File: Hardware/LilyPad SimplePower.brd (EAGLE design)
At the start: 28.4 x 28.4 mm, 20 parts, among them U1 MCP73831

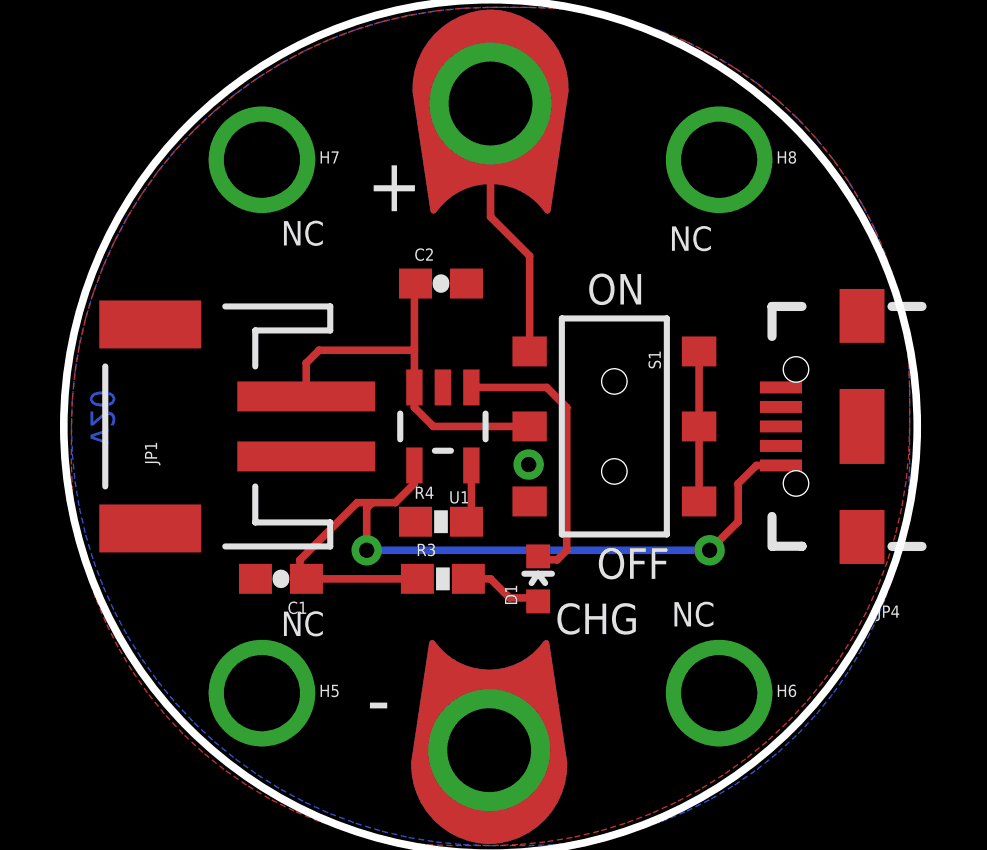
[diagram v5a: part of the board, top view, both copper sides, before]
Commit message: Updating bRestrict to give Lilypad petal pattern
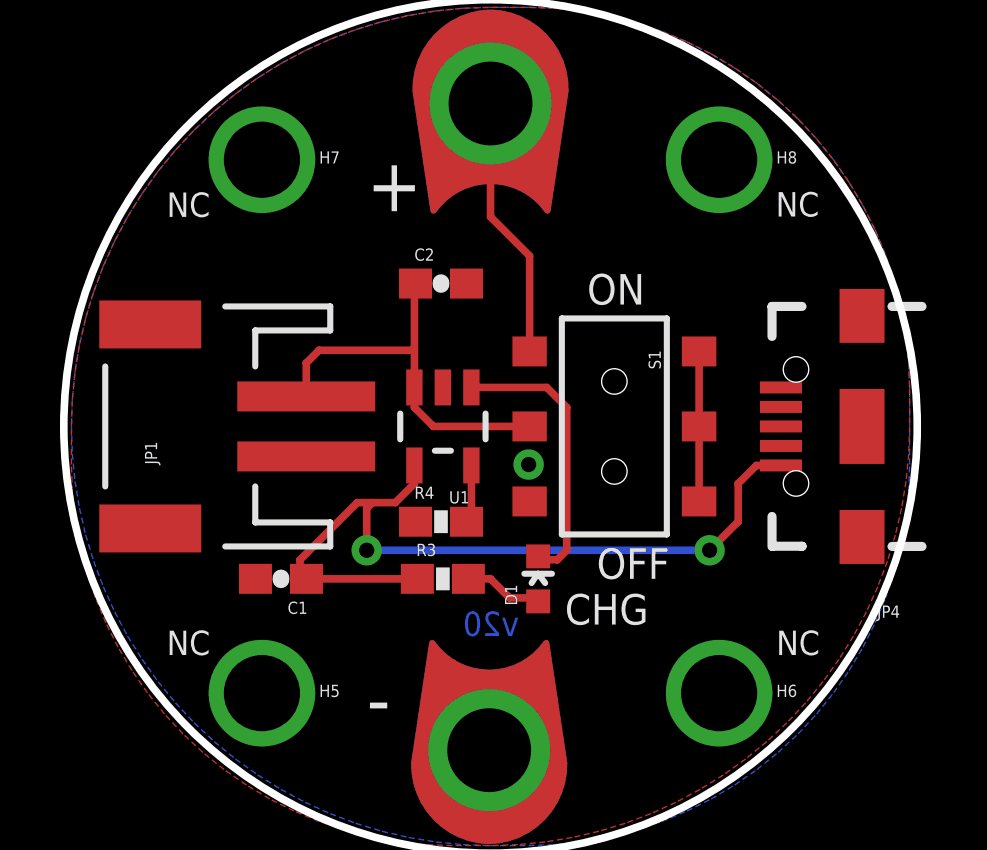
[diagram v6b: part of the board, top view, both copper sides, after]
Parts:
- moved JP3 0.81 mm to (6.51, -4.29)
- moved U$5 0.79 mm to (-5.24, -2.54)
- moved U$1 0.35 mm to (0.16, 1.91)
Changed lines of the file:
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@@
 <layer number="47" name="Measures" color="7" fill="1" visible="no" active="yes"/>
 <layer number="48" name="Document" color="7" fill="1" visible="no" active="yes"/>
-<layer number="49" name="Reference" color="7" fill="1" visible="yes" active="yes"/>
+<layer number="49" name="Reference" color="7" fill="1" visible="no" active="yes"/>
 <layer number="50" name="dxf" color="7" fill="1" visible="no" active="yes"/>
 <layer number="51" name="tDocu" color="6" fill="1" visible="yes" active="yes"/>
@@
 <text x="-4.1275" y="4.6355" size="1.778" layer="21" font="vector" ratio="15">+</text>
 <text x="6.35" y="-26.67" size="1.778" layer="51" font="vector">N. Seidle</text>
-<text x="-13.335" y="-3.175" size="0.8128" layer="16" font="vector" ratio="25" rot="SMR90">v20</text>
+<text x="0.9525" y="-9.525" size="0.8128" layer="16" font="vector" ratio="25" rot="SMR0">v20</text>
 <circle x="0" y="-2.54" radius="14.224" width="0.254" layer="20"/>
-<text x="2.159" y="-9.4615" size="1.016" layer="21" font="vector" ratio="15">CHG</text>
-<text x="-6.985" y="3.4925" size="0.8128" layer="21" font="vector" ratio="15">NC</text>
-<text x="6.0325" y="-9.2075" size="0.8128" layer="21" font="vector" ratio="15">NC</text>
+<text x="2.4765" y="-9.144" size="1.016" layer="21" font="vector" ratio="15">CHG</text>
+<text x="-10.795" y="4.445" size="0.8128" layer="21" font="vector" ratio="15">NC</text>
+<text x="9.525" y="-10.16" size="0.8128" layer="21" font="vector" ratio="15">NC</text>
 <text x="6.35" y="-29.21" size="1.778" layer="51" font="vector">Toni Klopfenstein</text>
-<text x="5.94995" y="3.3147" size="0.8128" layer="21" font="vector" ratio="15">NC</text>
-<text x="-6.985" y="-9.525" size="0.8128" layer="21" font="vector" ratio="15">NC</text>
+<text x="9.50595" y="4.4577" size="0.8128" layer="21" font="vector" ratio="15">NC</text>
+<text x="-10.795" y="-10.16" size="0.8128" layer="21" font="vector" ratio="15">NC</text>
 <text x="-4.1275" y="-12.5095" size="1.778" layer="21" font="vector" ratio="15">-</text>
 <wire x1="0" y1="12.065" x2="0" y2="-2.54" width="0" layer="47"/>
 <circle x="0" y="-2.54" radius="14.19903125" width="0.254" layer="30"/>
-<circle x="0" y="-2.54" radius="11.811" width="5.08" layer="42"/>
+<circle x="0" y="-2.54" radius="11.2776" width="6.096" layer="42"/>
+<circle x="-3.429" y="2.0955" radius="2.300015625" width="0.001" layer="49"/>
+<circle x="-5.3975" y="-4.7625" radius="2.300015625" width="0.001" layer="49"/>
+<circle x="-3.302" y="-7.4295" radius="2.300015625" width="0.001" layer="49"/>
+<circle x="0" y="-2.54" radius="8.128" width="0.0254" layer="49"/>
+<circle x="-5.6515" y="-0.9525" radius="2.300015625" width="0.001" layer="49"/>
+<circle x="3.556" y="1.9685" radius="2.300015625" width="0.001" layer="49"/>
+<circle x="5.6515" y="-1.143" radius="2.300015625" width="0.001" layer="49"/>
+<circle x="3.302" y="-7.366" radius="2.300015625" width="0.001" layer="49"/>
+<circle x="5.3975" y="-4.7625" radius="2.300015625" width="0.001" layer="49"/>
+<wire x1="-5.55625" y1="1.27" x2="-2.2225" y2="4.1275" width="0.0889" layer="42" curve="-149.184294"/>
+<wire x1="6.985" y1="-3.175" x2="7.3025" y2="-6.0325" width="0.0889" layer="42" curve="-84.400661"/>
+<wire x1="5.55625" y1="-7.14375" x2="2.06375" y2="-9.36625" width="0.0889" layer="42" curve="-130.939993"/>
+<wire x1="-2.06375" y1="-9.36625" x2="-5.55625" y2="-7.14375" width="0.0889" layer="42" curve="-130.432352"/>
+<wire x1="-5.55625" y1="-6.985" x2="-6.82625" y2="-3.01625" width="0.0889" layer="42" curve="-143.972627"/>
+<wire x1="1.74625" y1="4.445" x2="2.2225" y2="3.81" width="0.0889" layer="42" curve="-18.034286"/>
+<wire x1="2.38125" y1="3.96875" x2="5.715" y2="1.11125" width="0.0889" layer="42" curve="-146.382048"/>
+<wire x1="-2.06375" y1="4.1275" x2="-1.74625" y2="4.445" width="0.0889" layer="42"/>
+<wire x1="-6.82625" y1="-3.01625" x2="-5.55625" y2="1.42875" width="0.0889" layer="42" curve="-155.513319"/>
+<wire x1="5.715" y1="1.11125" x2="6.985" y2="-3.01625" width="0.0889" layer="42" curve="-141.555832"/>
 </plain>
 <attributes>
@@
 <element name="U$3" library="LilyPad-Wearables" package="PETAL-LONG-1-2SIDE" value="SEWTAP9" x="-0.04445" y="-13.3604" rot="R90"/>
 <element name="U$4" library="LilyPad-Wearables" package="PETAL-LONG-1-2SIDE" value="SEWTAP9" x="0" y="8.255" rot="R270"/>
-<element name="U$1" library="LilyPad-Wearables" package="LOGO-LILYPAD" value="LOGO-LPLP" x="0.3175" y="2.2225" rot="MR0"/>
-<element name="U$5" library="SparkFun-Aesthetics" package="OSHW-LOGO-S" value="OSHW-LOGOS" x="-6.0325" y="-2.54" rot="MR0"/>
-<element name="JP3" library="SparkFun-Aesthetics" package="SFE-LOGO-FLAME" value="LOGO-SFESK" x="5.715" y="-4.1275" rot="MR0"/>
+<element name="U$1" library="LilyPad-Wearables" package="LOGO-LILYPAD" value="LOGO-LPLP" x="0.15875" y="1.905" rot="MR0"/>
+<element name="U$5" library="SparkFun-Aesthetics" package="OSHW-LOGO-S" value="OSHW-LOGOS" x="-5.23875" y="-2.54" rot="MR0"/>
+<element name="JP3" library="SparkFun-Aesthetics" package="SFE-LOGO-FLAME" value="LOGO-SFESK" x="6.50875" y="-4.28625" rot="MR0"/>
 <element name="U1" library="SparkFun-PowerIC" package="SOT23-5" value="MCP73831" x="-1.5875" y="-2.54" rot="R180">
 <attribute name="PROD_ID" value="IC-09995" x="-1.5875" y="-2.54" size="1.778" layer="27" font="vector" ratio="15" rot="R180" display="off"/>

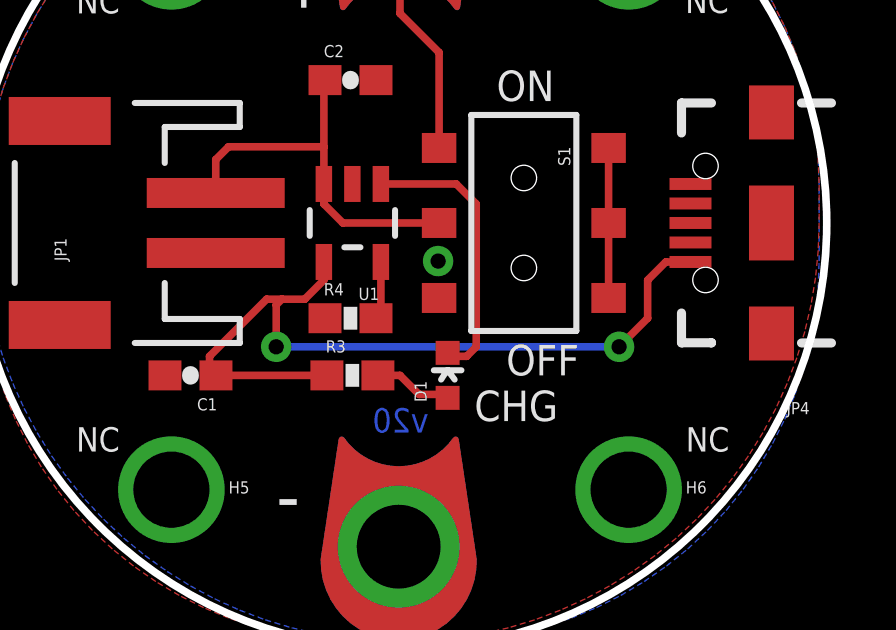
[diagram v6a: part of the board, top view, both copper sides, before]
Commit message: Updating minor fixes for acid traps
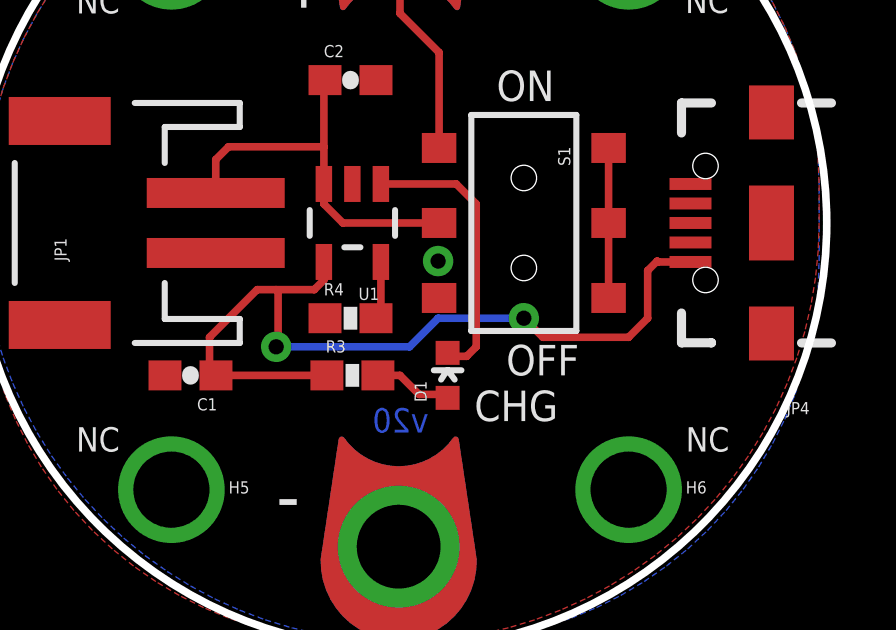
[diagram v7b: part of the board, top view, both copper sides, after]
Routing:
- net N$3: track 27.3 -> 28.7 mm
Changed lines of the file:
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@@
 <setting verticaltext="up"/>
 </settings>
-<grid distance="0.05" unitdist="inch" unit="inch" style="lines" multiple="1" display="yes" altdistance="0.005" altunitdist="inch" altunit="inch"/>
+<grid distance="0.0125" unitdist="inch" unit="inch" style="lines" multiple="1" display="yes" altdistance="0.005" altunitdist="inch" altunit="inch"/>
 <layers>
 <layer number="1" name="Top" color="4" fill="1" visible="yes" active="yes"/>
@@
 <wire x1="-6.135" y1="-7.62" x2="-2.4375" y2="-7.62" width="0.254" layer="1"/>
 <wire x1="-2.5375" y1="-3.8401" x2="-2.5375" y2="-4.4425" width="0.254" layer="1"/>
-<wire x1="-2.5375" y1="-4.4425" x2="-3.175" y2="-5.08" width="0.254" layer="1"/>
-<wire x1="-3.175" y1="-5.08" x2="-3.937" y2="-5.08" width="0.254" layer="1"/>
-<wire x1="-3.937" y1="-5.08" x2="-4.445" y2="-5.08" width="0.254" layer="1"/>
-<wire x1="-4.445" y1="-5.08" x2="-6.35" y2="-6.985" width="0.254" layer="1"/>
-<wire x1="-6.35" y1="-6.985" x2="-6.35" y2="-7.405" width="0.254" layer="1"/>
 <wire x1="-6.35" y1="-7.405" x2="-6.135" y2="-7.62" width="0.254" layer="1"/>
-<wire x1="9.6825" y1="-3.84" x2="8.86" y2="-3.84" width="0.254" layer="1"/>
-<wire x1="8.86" y1="-3.84" x2="8.255" y2="-4.445" width="0.254" layer="1"/>
-<wire x1="8.255" y1="-4.445" x2="8.255" y2="-5.715" width="0.254" layer="1"/>
-<wire x1="8.255" y1="-5.715" x2="7.3025" y2="-6.6675" width="0.254" layer="1"/>
-<via x="7.3025" y="-6.6675" extent="1-16" drill="0.508"/>
-<wire x1="7.3025" y1="-6.6675" x2="-4.1275" y2="-6.6675" width="0.254" layer="16"/>
+<via x="4.1275" y="-5.715" extent="1-16" drill="0.508"/>
 <via x="-4.1275" y="-6.6675" extent="1-16" drill="0.508"/>
-<wire x1="-4.1275" y1="-6.6675" x2="-4.1275" y2="-5.2705" width="0.254" layer="1"/>
-<wire x1="-4.1275" y1="-5.2705" x2="-3.937" y2="-5.08" width="0.254" layer="1"/>
+<wire x1="-6.35" y1="-7.405" x2="-6.35" y2="-6.35" width="0.254" layer="1"/>
+<wire x1="-6.35" y1="-6.35" x2="-4.7625" y2="-4.7625" width="0.254" layer="1"/>
+<wire x1="-4.064" y1="-4.826" x2="-4.064" y2="-6.604" width="0.254" layer="1"/>
+<wire x1="-4.064" y1="-6.604" x2="-4.1275" y2="-6.6675" width="0.254" layer="1"/>
+<wire x1="-2.8575" y1="-4.7625" x2="-2.5375" y2="-4.4425" width="0.254" layer="1"/>
+<wire x1="-4.7625" y1="-4.7625" x2="-4.1275" y2="-4.7625" width="0.254" layer="1"/>
+<wire x1="-4.1275" y1="-4.7625" x2="-2.8575" y2="-4.7625" width="0.254" layer="1"/>
+<wire x1="-4.064" y1="-4.826" x2="-4.1275" y2="-4.7625" width="0.254" layer="1"/>
+<wire x1="8.255" y1="-5.715" x2="7.62" y2="-6.35" width="0.254" layer="1"/>
+<wire x1="7.62" y1="-6.35" x2="4.7625" y2="-6.35" width="0.254" layer="1"/>
+<wire x1="4.7625" y1="-6.35" x2="4.1275" y2="-5.715" width="0.254" layer="1"/>
+<wire x1="9.6825" y1="-3.84" x2="8.6025" y2="-3.84" width="0.254" layer="1"/>
+<wire x1="8.6025" y1="-3.84" x2="8.5725" y2="-3.81" width="0.254" layer="1"/>
+<wire x1="8.5725" y1="-3.81" x2="8.255" y2="-4.1275" width="0.254" layer="1"/>
+<wire x1="8.255" y1="-4.1275" x2="8.255" y2="-5.715" width="0.254" layer="1"/>
+<wire x1="-4.1275" y1="-6.6675" x2="0.3175" y2="-6.6675" width="0.254" layer="16"/>
+<wire x1="0.3175" y1="-6.6675" x2="1.27" y2="-5.715" width="0.254" layer="16"/>
+<wire x1="1.27" y1="-5.715" x2="4.1275" y2="-5.715" width="0.254" layer="16"/>
 </signal>
 <signal name="N$4">

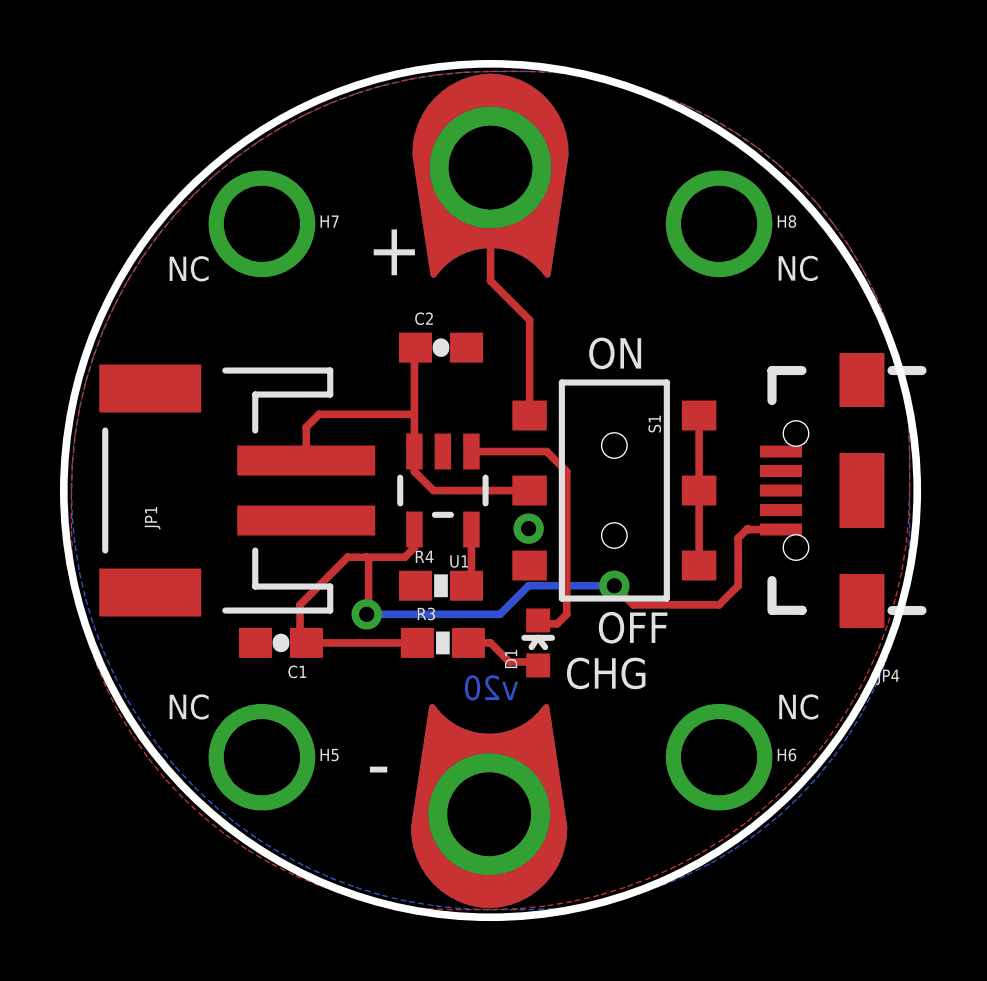
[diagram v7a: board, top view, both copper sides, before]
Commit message: Updating board with more classic LilyPad design
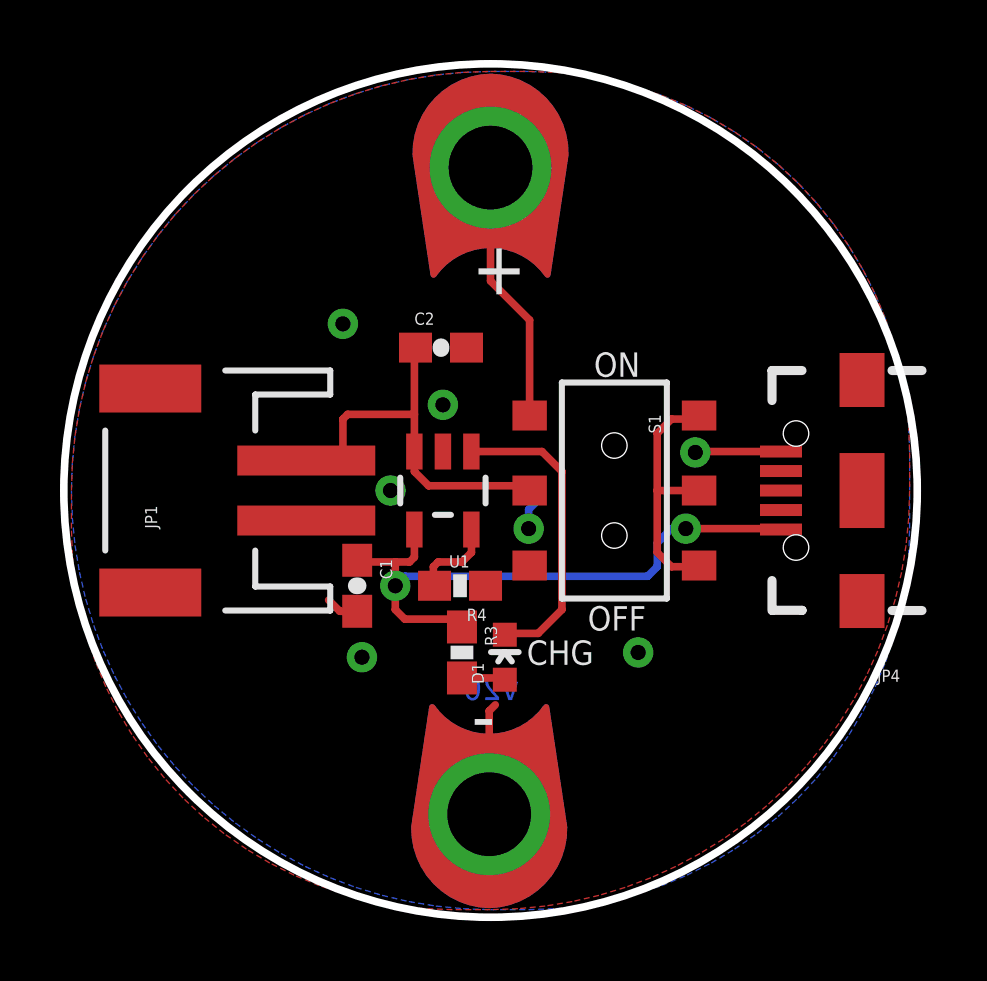
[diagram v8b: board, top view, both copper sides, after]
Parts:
- removed H5, H6, H7, H8: SEW_HOLE, LilyPad-Wearables:SIMPLE_HOLE
- moved C1 3.17 mm to (-4.45, -5.71), turned to 270 degrees
- moved D1 1.21 mm to (0.48, -8.10)
- moved R3 0.71 mm to (-0.95, -7.94), turned to 270 degrees
- moved U$1 0.65 mm to (0.00, 1.27)
- moved R4 0.64 mm to (-1.02, -5.71), turned to 180 degrees
- moved U$5 0.32 mm to (-5.56, -2.54)
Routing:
- net GND: track 0.00 -> 7.64 mm, vias 1 -> 7
- net N$3: track 28.7 -> 21.1 mm
- net SINK1: track 5.00 -> 8.62 mm
- net N$5: track 2.64 -> 1.45 mm
- net N$7: track 1.94 -> 2.88 mm
- net N$4: track 9.35 -> 10.1 mm
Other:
- board text removed: "NC"
